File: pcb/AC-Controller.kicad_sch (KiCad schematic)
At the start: 31 parts, among them J1 Serial, Q1 AO3400A, SW1 Mode, SW2 Value, SW3 RESET, U1 ESP32-WROOM-32

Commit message: feat: remove battery protection IC
Since I only use protected battery packs (which is highly recommended) the additional protection IC on the PCB was obsolete and only raised production cost.
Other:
- moved on the sheet: D1, R11
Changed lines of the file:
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@@
     (stroke (width 0) (type default))
   )
-  (wire (pts (xy 123.19 92.71) (xy 123.19 95.25))
+  (wire (pts (xy 114.3 92.71) (xy 114.3 95.25))
     (stroke (width 0) (type default))
   )
@@
     (stroke (width 0) (type default))
   )
-  (wire (pts (xy 123.19 100.33) (xy 123.19 102.87))
+  (wire (pts (xy 114.3 100.33) (xy 114.3 102.87))
     (stroke (width 0) (type default))
   )
@@
     (stroke (width 0) (type default))
   )
-  (wire (pts (xy 123.19 85.09) (xy 123.19 87.63))
+  (wire (pts (xy 114.3 85.09) (xy 114.3 87.63))
     (stroke (width 0) (type default))
   )
@@
     (effects (font (size 1.27 1.27)) (justify left bottom))
   )
-  (label "LED" (at 123.19 85.09 90) (fields_autoplaced)
+  (label "LED" (at 114.3 85.09 90) (fields_autoplaced)
     (effects (font (size 1.27 1.27)) (justify left bottom))
   )
@@
     )
   )
-  (symbol (lib_id "Device:LED_Small") (at 123.19 97.79 90) (unit 1)
-    (in_bom yes) (on_board yes) (dnp no) (fields_autoplaced)
-    (property "Reference" "D1" (at 124.968 96.7025 90)
+  (symbol (lib_id "Device:LED_Small") (at 114.3 97.79 90) (unit 1)
+    (in_bom yes) (on_board yes) (dnp no) (fields_autoplaced)
+    (property "Reference" "D1" (at 116.078 96.7025 90)
       (effects (font (size 1.27 1.27)) (justify right))
     )
-    (property "Value" "Status" (at 124.968 98.7505 90)
+    (property "Value" "Status" (at 116.078 98.7505 90)
       (effects (font (size 1.27 1.27)) (justify right))
     )
-    (property "Footprint" "LED_SMD:LED_0603_1608Metric" (at 123.19 97.79 90)
-      (effects (font (size 1.27 1.27)) hide)
-    )
-    (property "Datasheet" "~" (at 123.19 97.79 90)
-      (effects (font (size 1.27 1.27)) hide)
-    )
-    (property "LCSC" "C2286" (at 123.19 97.79 0)
+    (property "Footprint" "LED_SMD:LED_0603_1608Metric" (at 114.3 97.79 90)
+      (effects (font (size 1.27 1.27)) hide)
+    )
+    (property "Datasheet" "~" (at 114.3 97.79 90)
+      (effects (font (size 1.27 1.27)) hide)
+    )
+    (property "LCSC" "C2286" (at 114.3 97.79 0)
       (effects (font (size 1.27 1.27)) hide)
     )
@@
     )
   )
-  (symbol (lib_id "power:GND") (at 123.19 102.87 0) (unit 1)
-    (in_bom yes) (on_board yes) (dnp no) (fields_autoplaced)
-    (property "Reference" "#PWR020" (at 123.19 109.22 0)
-      (effects (font (size 1.27 1.27)) hide)
-    )
-    (property "Value" "GND" (at 123.19 106.815 0)
-      (effects (font (size 1.27 1.27)))
-    )
-    (property "Footprint" "" (at 123.19 102.87 0)
-      (effects (font (size 1.27 1.27)) hide)
-    )
-    (property "Datasheet" "" (at 123.19 102.87 0)
+  (symbol (lib_id "power:GND") (at 114.3 102.87 0) (unit 1)
+    (in_bom yes) (on_board yes) (dnp no) (fields_autoplaced)
+    (property "Reference" "#PWR020" (at 114.3 109.22 0)
+      (effects (font (size 1.27 1.27)) hide)
+    )
+    (property "Value" "GND" (at 114.3 106.815 0)
+      (effects (font (size 1.27 1.27)))
+    )
+    (property "Footprint" "" (at 114.3 102.87 0)
+      (effects (font (size 1.27 1.27)) hide)
+    )
+    (property "Datasheet" "" (at 114.3 102.87 0)
       (effects (font (size 1.27 1.27)) hide)
     )
@@
     )
   )
-  (symbol (lib_id "Device:R_Small") (at 123.19 90.17 0) (unit 1)
-    (in_bom yes) (on_board yes) (dnp no) (fields_autoplaced)
-    (property "Reference" "R11" (at 124.6886 89.146 0)
-      (effects (font (size 1.27 1.27)) (justify left))
-    )
-    (property "Value" "680R" (at 124.6886 91.194 0)
-      (effects (font (size 1.27 1.27)) (justify left))
-    )
-    (property "Footprint" "Resistor_SMD:R_0603_1608Metric" (at 123.19 90.17 0)
-      (effects (font (size 1.27 1.27)) hide)
-    )
-    (property "Datasheet" "~" (at 123.19 90.17 0)
-      (effects (font (size 1.27 1.27)) hide)
-    )
-    (property "LCSC" "C23228" (at 123.19 90.17 0)
-      (effects (font (size 1.27 1.27)) hide)
-    )
+  (symbol (lib_id "Device:R_Small") (at 114.3 90.17 0) (unit 1)
+    (in_bom yes) (on_board yes) (dnp no) (fields_autoplaced)
+    (property "Reference" "R11" (at 115.7986 89.146 0)
+      (effects (font (size 1.27 1.27)) (justify left))
+    )
+    (property "Value" "680R" (at 115.7986 91.194 0)
+      (effects (font (size 1.27 1.27)) (justify left))
+    )
+    (property "Footprint" "Resistor_SMD:R_0603_1608Metric" (at 114.3 90.17 0)
+      (effects (font (size 1.27 1.27)) hide)
+    )
+    (property "Datasheet" "~" (at 114.3 90.17 0)
+      (effects (font (size 1.27 1.27)) hide)
+    )
+    (property "LCSC" "C23228" (at 114.3 90.17 0)
+      (effects (font (size 1.27 1.27)) hide)
+    )

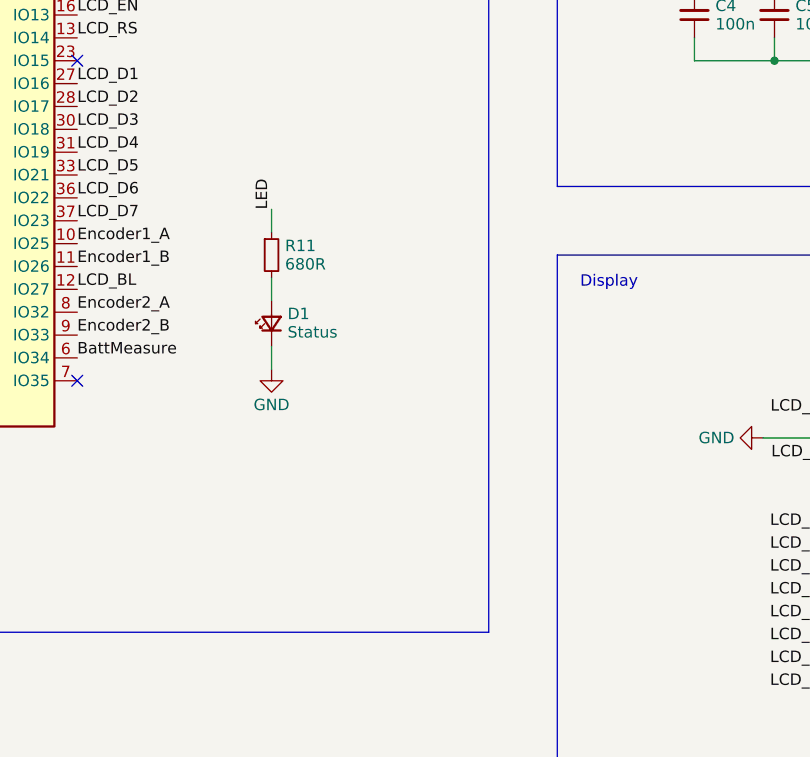
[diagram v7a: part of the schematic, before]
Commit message: feat: add charging indicator LED
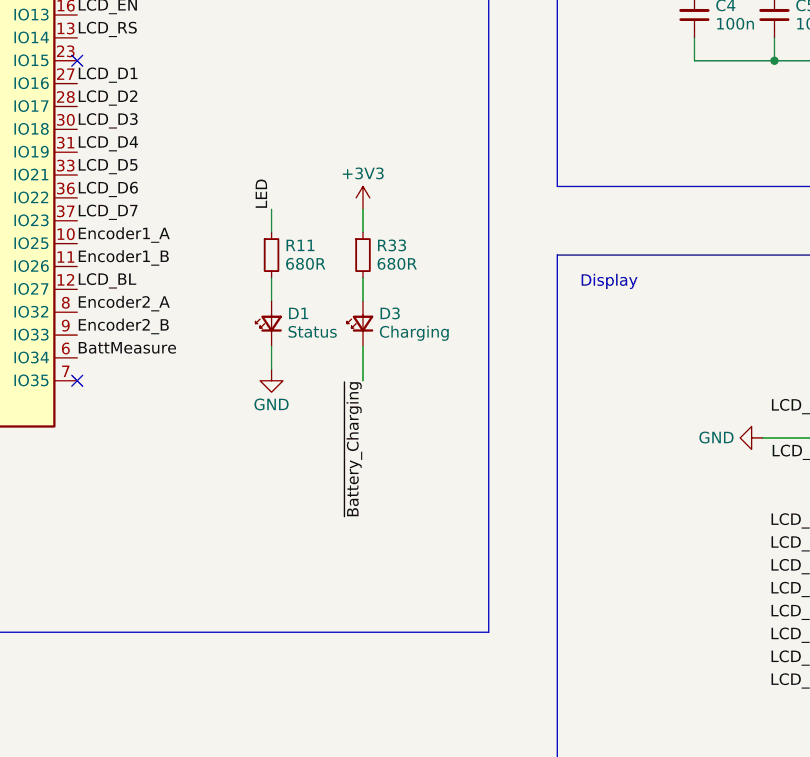
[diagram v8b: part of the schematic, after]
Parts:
- added D3: Charging, LED_SMD:LED_0603_1608Metric, symbol Device:LED_Small
- added R33: 680R, Resistor_SMD:R_0402_1005Metric, symbol Device:R_Small
- R11: footprint Resistor_SMD:R_0603_1608Metric -> Resistor_SMD:R_0402_1005Metric; LCSC C23228 -> C25130
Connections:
- net +3V3: now also R33.1
- net ~{Battery_Charging}: now also D3.1 (K)
- new net: D3.2 (A), R33.2
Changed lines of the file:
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@@
+    (stroke (width 0) (type default))
+  )
+  (wire (pts (xy 124.46 92.71) (xy 124.46 95.25))
     (stroke (width 0) (type default))
   )
@@
     (stroke (width 0) (type default))
   )
+  (wire (pts (xy 124.46 100.33) (xy 124.46 104.14))
+    (stroke (width 0) (type default))
+  )
   (wire (pts (xy 113.03 181.61) (xy 105.41 181.61))
     (stroke (width 0) (type default))
@@
   )
   (wire (pts (xy 214.63 148.59) (xy 214.63 146.05))
+    (stroke (width 0) (type default))
+  )
+  (wire (pts (xy 124.46 85.09) (xy 124.46 87.63))
     (stroke (width 0) (type default))
   )
@@
     (effects (font (size 1.27 1.27)) (justify right bottom))
   )
+  (label "~{Battery_Charging}" (at 124.46 104.14 270) (fields_autoplaced)
+    (effects (font (size 1.27 1.27)) (justify right bottom))
+  )
   (label "Encoder1_B" (at 158.75 58.42 180) (fields_autoplaced)
     (effects (font (size 1.27 1.27)) (justify right bottom))
@@
   (label "Button2" (at 92.71 58.42 0) (fields_autoplaced)
     (effects (font (size 1.27 1.27)) (justify left bottom))
+  )
+  (symbol (lib_id "Device:LED_Small") (at 124.46 97.79 90) (unit 1)
+    (in_bom yes) (on_board yes) (dnp no) (fields_autoplaced)
+    (property "Reference" "D3" (at 126.238 96.7025 90)
+      (effects (font (size 1.27 1.27)) (justify right))
+    )
+    (property "Value" "Charging" (at 126.238 98.7505 90)
+      (effects (font (size 1.27 1.27)) (justify right))
+    )
+    (property "Footprint" "LED_SMD:LED_0603_1608Metric" (at 124.46 97.79 90)
+      (effects (font (size 1.27 1.27)) hide)
+    )
+    (property "Datasheet" "~" (at 124.46 97.79 90)
+      (effects (font (size 1.27 1.27)) hide)
+    )
+    (property "LCSC" "C2286" (at 124.46 97.79 0)
+      (effects (font (size 1.27 1.27)) hide)
+    )
+    (pin "1")
+    (pin "2")
+    (instances
+      (project "AC-Controller"
+        (path "/a9b77c2b-ed0c-4412-867d-4d65898d0fc4"
+          (reference "D3") (unit 1)
+        )
+      )
+    )
   )
   (symbol (lib_id "power:GND") (at 214.63 148.59 0) (unit 1)
@@
       (effects (font (size 1.27 1.27)) (justify left))
     )
-    (property "Footprint" "Resistor_SMD:R_0603_1608Metric" (at 114.3 90.17 0)
+    (property "Footprint" "Resistor_SMD:R_0402_1005Metric" (at 114.3 90.17 0)
       (effects (font (size 1.27 1.27)) hide)
     )
@@
       (effects (font (size 1.27 1.27)) hide)
     )
-    (property "LCSC" "C23228" (at 114.3 90.17 0)
+    (property "LCSC" "C25130" (at 114.3 90.17 0)
       (effects (font (size 1.27 1.27)) hide)
     )
@@
         (path "/a9b77c2b-ed0c-4412-867d-4d65898d0fc4"
           (reference "C2") (unit 1)
+        )
+      )
+    )
+  )
+  (symbol (lib_id "Device:R_Small") (at 124.46 90.17 0) (unit 1)
+    (in_bom yes) (on_board yes) (dnp no) (fields_autoplaced)
+    (property "Reference" "R33" (at 125.9586 89.146 0)
+      (effects (font (size 1.27 1.27)) (justify left))
+    )
+    (property "Value" "680R" (at 125.9586 91.194 0)
+      (effects (font (size 1.27 1.27)) (justify left))
+    )
+    (property "Footprint" "Resistor_SMD:R_0402_1005Metric" (at 124.46 90.17 0)
+      (effects (font (size 1.27 1.27)) hide)
+    )
+    (property "Datasheet" "~" (at 124.46 90.17 0)
+      (effects (font (size 1.27 1.27)) hide)
+    )
+    (property "LCSC" "C25130" (at 124.46 90.17 0)
+      (effects (font (size 1.27 1.27)) hide)
+    )
+    (pin "1")
+    (pin "2")
+    (instances
+      (project "AC-Controller"
+        (path "/a9b77c2b-ed0c-4412-867d-4d65898d0fc4"
+          (reference "R33") (unit 1)
         )
       )
@@
         )
       )
+    )
+  )
+  (symbol (lib_id "power:+3V3") (at 124.46 85.09 0) (unit 1)
+    (in_bom yes) (on_board yes) (dnp no) (fields_autoplaced)
+    (property "Reference" "#PWR038" (at 124.46 88.9 0)
+      (effects (font (size 1.27 1.27)) hide)
+    )
+    (property "Value" "+3V3" (at 124.46 81.145 0)
+      (effects (font (size 1.27 1.27)))
+    )
+    (property "Footprint" "" (at 124.46 85.09 0)
+      (effects (font (size 1.27 1.27)) hide)
+    )
+    (property "Datasheet" "" (at 124.46 85.09 0)
+      (effects (font (size 1.27 1.27)) hide)
+    )
+    (pin "1")
+    (instances
+      (project "AC-Controller"
+        (path "/a9b77c2b-ed0c-4412-867d-4d65898d0fc4"
+          (reference "#PWR038") (unit 1)
+        )
+      )
